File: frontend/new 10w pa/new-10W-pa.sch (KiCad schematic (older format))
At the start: 41 parts, among them CN1 BREAKOUT, K1 D3002, P1 CONN_01X02, P2 CONN_02X01, P3 External 12V-13.8V (OSTTC0221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, P4 CONN_01X02, P5 CONN_01X02, Q1 FDV301, Q2 FDV301, Q3 RD16HHF1, T1 TRANSFO, T2 OUT_TRANSF, U1 4050, U6 LP2951-50D, U7 LP2951-50D

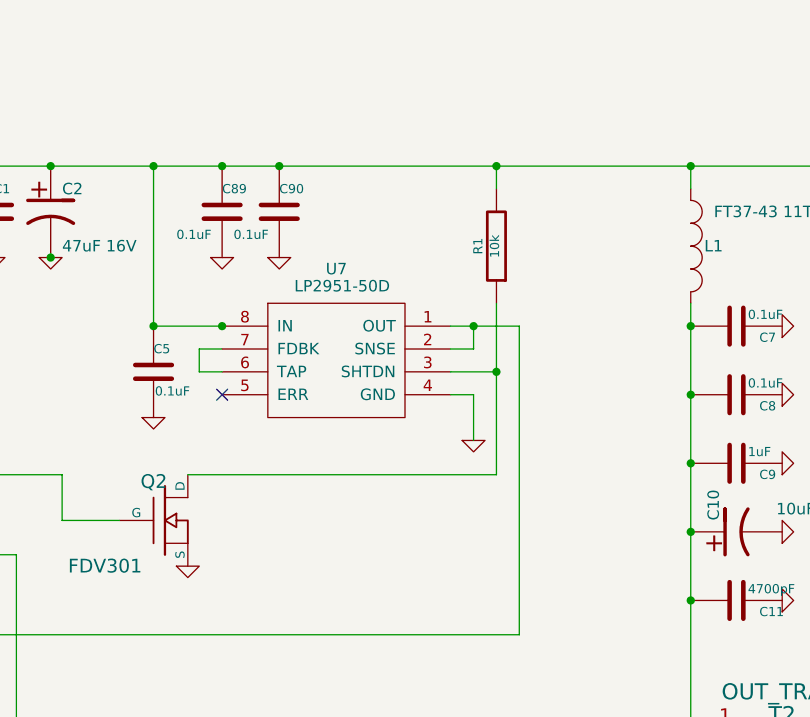
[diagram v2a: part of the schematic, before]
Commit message: modify mounting holes
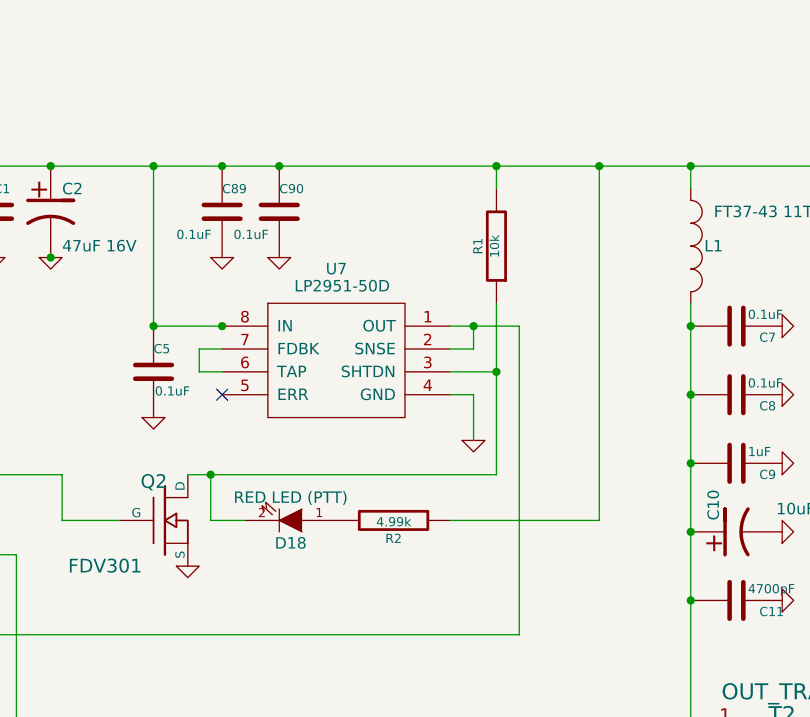
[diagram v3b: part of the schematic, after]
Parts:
- added D18: RED LED (PTT), LEDs:LED-0805, symbol LED
- added R2: 4.99k, HERMESLITE:R_0805, symbol R
- Q1, Q2: footprint SMD_Packages:SOT-23-GDS -> HERMESLITE:SOT-23-GDS
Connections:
- net +12V: now also R2.1
- net at Q2.D, R1.1, U7.3 (SHTDN): now also D18.2 (K)
- new net: D18.1 (A), R2.2

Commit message: first pass for Oshpark
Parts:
- removed CN1: BREAKOUT, HERMESLITE:BREAKOUT, symbol BREAKOUT
- removed U1: 4050, Housings_SOIC:SOIC-16_3.9x9.9mm_Pitch1.27mm, symbol 4050
- added C93, C94: 0.1uF, HERMESLITE:C_0805, symbol C
- added D19, D20: DIODE, Diodes_SMD:Diode-SMA_Standard, symbol DIODE
- added P7: Control from MegaBasic, Pin_Headers:Pin_Header_Straight_1x07, symbol CONN_01X07
- added P8: F/R to Hermes Lite, Pin_Headers:Pin_Header_Straight_1x03, symbol CONN_01X03
- added R11, R3, R4, R9: 470, HERMESLITE:R_0805, symbol R
- added R12, R22, R7, R8: 100 .37W, HERMESLITE:R_0805, symbol R
- added T3: F-R-XFMR, HERMESLITE:F_R_Transf, symbol F-R-XFMR
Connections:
- net A: now also P7.6 (P6)
- net B: now also P7.5 (P5)
- net C: now also P7.4 (P4)
- net D: now also P7.3 (P3)
- net GND: now also C93.2, C94.2, P7.1 (P1), P7.7 (P7), P8.1 (P1), R12.2, R22.2, R3.2, R4.2, R7.2, R8.2, T3.6, T3.8
- net TXOUT: now also T3.3, T3.5; no longer K1.4 (T1)
- net at Q2.G: now also P7.2 (P2)
- net VCC renamed 5V
- new net: K1.4 (T1), T3.4
- new net: D20.1 (A), R12.1, R22.1, T3.1, T3.7
- new net: D19.1 (A), R7.1, R8.1, T3.2
- new net: C94.1, D20.2 (K), R11.1
- new net: P8.3 (P3), R11.2, R4.1
- new net: C93.1, D19.2 (K), R9.1
- new net: P8.2 (P2), R3.1, R9.2
- no-connect marks 9 -> 3
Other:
- note added: "FWD"
- note added: "REV"
- note added: "Voltage divider values are TBD, starting with a 50% reduction..."

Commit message: updates
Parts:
- removed Q1: FDV301, HERMESLITE:SOT-23-GDS, symbol MOS_N
- removed R12, R22, R7: 100 .37W, HERMESLITE:R_0805, symbol R
- removed T3: F-R-XFMR, HERMESLITE:F_R_Transf, symbol F-R-XFMR
- removed U7: LP2951-50D, Housings_SOIC:SOIC-8_3.9x4.9mm_Pitch1.27mm, symbol LP2951-50D
- added C95: 0.01uF, HERMESLITE:C_0805, symbol C
- added C96: 1uF, HERMESLITE:C_0805, symbol C
- added T3, T4: PWR_TRANS, symbol PWR_TRANS
- C5, C93, C94: value 0.1uF -> 0.01uF
- C87: value 0.1uF -> 1uF
- D19, D20: value DIODE -> 1n5711
- R1: value 10k -> 150k
- R11, R9: value 470 -> 3.3k
- R3: value 470 -> 51
- R4: value 470 -> 150k
- R8: value 100 .37W -> 51
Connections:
- net +12V: no longer C5.1, R1.2
- net 5V: now also K1.8 (C2), C96.1
- net GND: now also C5.1, C93.1, R1.1, R8.1, C95.2, C96.2, T3.3 (SB), T4.3 (SB); no longer C5.2, C93.2, R8.2
- net TXOUT: now also T3.2 (AB), T4.4 (SA)
- net at K1.10 (-): now also D18.2 (K), Q2.D
- net at K1.4 (T1): now also T3.1 (AA)
- net at D20.1 (A): now also R3.1, T3.4 (SA), T4.2 (AB)
- net at D19.1 (A): now also R8.2, T4.1 (AA); no longer R8.1
- net at C94.1, D20.2 (K): now also R11.2; no longer R11.1
- net at P8.3 (P3), R4.1: now also R11.1, C95.1; no longer R11.2
- new net: C93.2, D19.2 (K), R9.2
- new net: P8.2 (P2), R1.2, R9.1
- no-connect marks 3 -> 2
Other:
- note removed: "Voltage divider values are TBD, starting with a 50% reduction..."
- moved on the sheet: C93, C94, D19, D20, P8, R11, R8, R9
